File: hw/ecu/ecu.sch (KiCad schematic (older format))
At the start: 66 parts, among them J1 POWER, J2 UART_DEBUG, J3 DEBUG, J4 EXPANSION, J5 SWD, J6 CAN, J7 USB_B_Micro, SW1 RESET, U1 M24C64, U2 STM32F072RBTx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

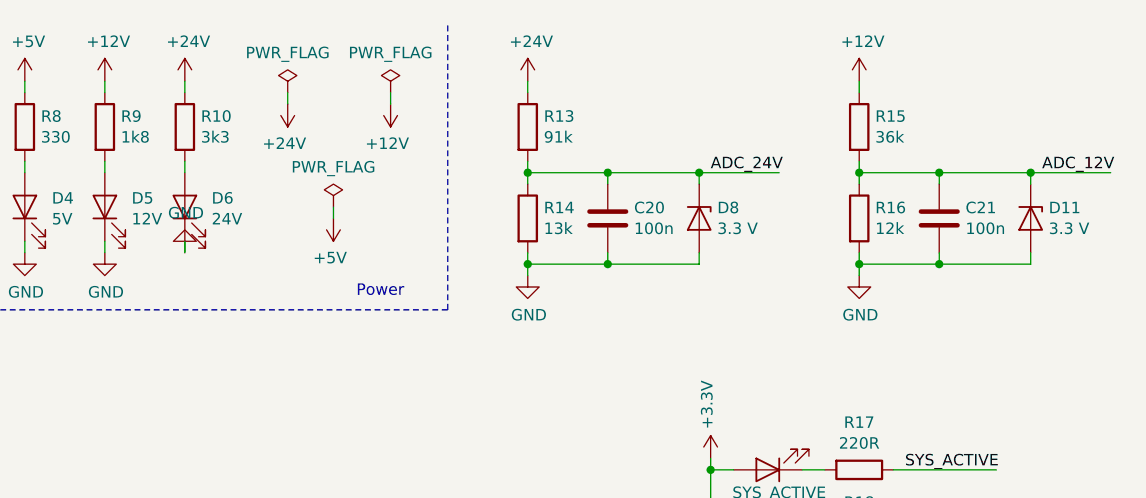
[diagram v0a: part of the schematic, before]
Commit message: Updated few resistors/capacitors values on board
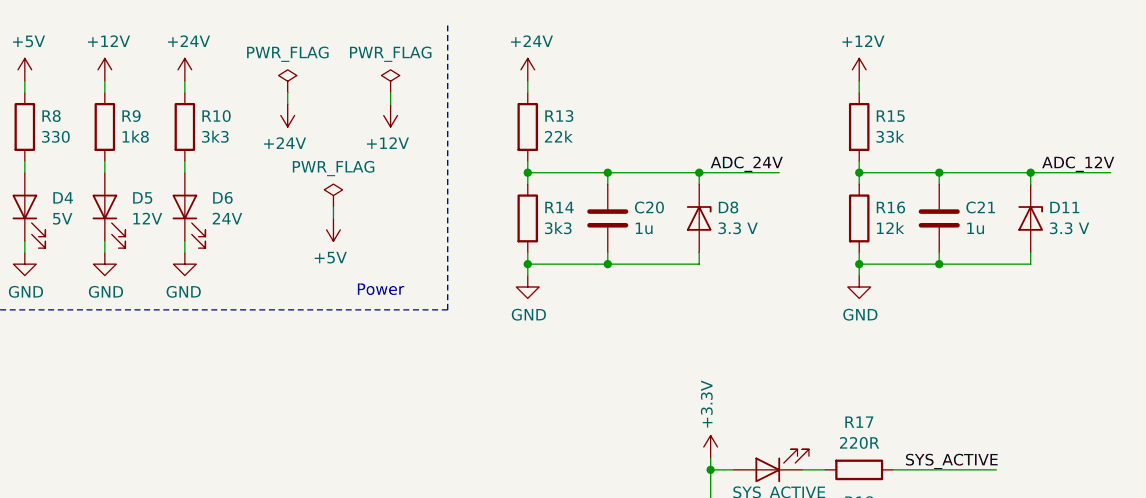
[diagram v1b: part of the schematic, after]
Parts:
- C20, C21: value 100n -> 1u
- R13: value 91k -> 22k
- R14: value 13k -> 3k3
- R15: value 36k -> 33k
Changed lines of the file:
@@
 F 3 "" H 7100 1500 50  0001 C CNN
 	1    7100 1500
-	1    0    0    1
+	-1   0    0    -1
 $EndComp
 Wire Wire Line
@@
 P 8600 950
 F 0 "R13" H 8670 996 50  0000 L CNN
-F 1 "91k" H 8670 905 50  0000 L CNN
+F 1 "22k" H 8670 905 50  0000 L CNN
 F 2 "Resistor_SMD:R_0805_2012Metric" V 8530 950 50  0001 C CNN
 F 3 "~" H 8600 950 50  0001 C CNN
@@
 P 8600 1350
 F 0 "R14" H 8670 1396 50  0000 L CNN
-F 1 "13k" H 8670 1305 50  0000 L CNN
+F 1 "3k3" H 8670 1305 50  0000 L CNN
 F 2 "Resistor_SMD:R_0805_2012Metric" V 8530 1350 50  0001 C CNN
 F 3 "~" H 8600 1350 50  0001 C CNN
@@
 P 8950 1350
 F 0 "C20" H 9065 1396 50  0000 L CNN
-F 1 "100n" H 9065 1305 50  0000 L CNN
+F 1 "1u" H 9065 1305 50  0000 L CNN
 F 2 "Capacitor_SMD:C_0805_2012Metric" H 8988 1200 50  0001 C CNN
 F 3 "~" H 8950 1350 50  0001 C CNN
@@
 P 10050 950
 F 0 "R15" H 10120 996 50  0000 L CNN
-F 1 "36k" H 10120 905 50  0000 L CNN
+F 1 "33k" H 10120 905 50  0000 L CNN
 F 2 "Resistor_SMD:R_0805_2012Metric" V 9980 950 50  0001 C CNN
 F 3 "~" H 10050 950 50  0001 C CNN
@@
 P 10400 1350
 F 0 "C21" H 10515 1396 50  0000 L CNN
-F 1 "100n" H 10515 1305 50  0000 L CNN
+F 1 "1u" H 10515 1305 50  0000 L CNN
 F 2 "Capacitor_SMD:C_0805_2012Metric" H 10438 1200 50  0001 C CNN
 F 3 "~" H 10400 1350 50  0001 C CNN

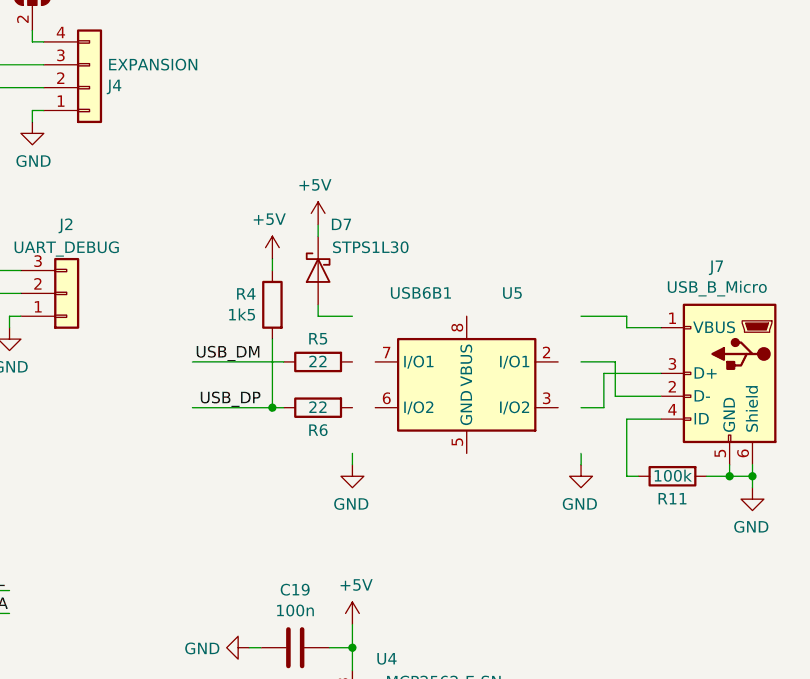
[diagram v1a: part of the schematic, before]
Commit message: Updated schematic to latest changes in usb protection ic
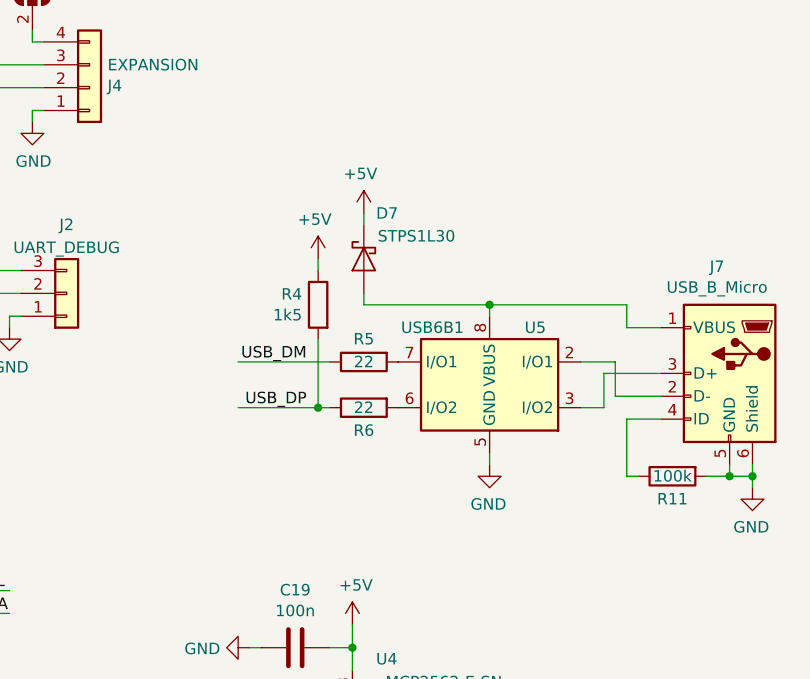
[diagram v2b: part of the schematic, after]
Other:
- moved on the sheet: D7, R4, R5, R6, U5
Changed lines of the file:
@@
 L Device:R R5
 U 1 1 5BB485B5
-P 5750 3700
-F 0 "R5" V 5650 3700 50  0000 C CNN
-F 1 "22" V 5750 3700 50  0000 C CNN
-F 2 "Resistor_SMD:R_0805_2012Metric" V 5680 3700 50  0001 C CNN
-F 3 "~" H 5750 3700 50  0001 C CNN
-	1    5750 3700
+P 5950 3700
+F 0 "R5" V 5850 3700 50  0000 C CNN
+F 1 "22" V 5950 3700 50  0000 C CNN
+F 2 "Resistor_SMD:R_0805_2012Metric" V 5880 3700 50  0001 C CNN
+F 3 "~" H 5950 3700 50  0001 C CNN
+	1    5950 3700
 	0    -1   1    0
 $EndComp
@@
 L Device:R R6
 U 1 1 5BB48786
-P 5750 3900
-F 0 "R6" V 5850 3900 50  0000 C CNN
-F 1 "22" V 5750 3900 50  0000 C CNN
-F 2 "Resistor_SMD:R_0805_2012Metric" V 5680 3900 50  0001 C CNN
-F 3 "~" H 5750 3900 50  0001 C CNN
-	1    5750 3900
+P 5950 3900
+F 0 "R6" V 6050 3900 50  0000 C CNN
+F 1 "22" V 5950 3900 50  0000 C CNN
+F 2 "Resistor_SMD:R_0805_2012Metric" V 5880 3900 50  0001 C CNN
+F 3 "~" H 5950 3900 50  0001 C CNN
+	1    5950 3900
 	0    -1   1    0
 $EndComp
-Text Label 5500 3700 2    50   ~ 0
+Text Label 5700 3700 2    50   ~ 0
 USB_DM
 Wire Wire Line
-	5600 3900 5550 3900
-Text Label 5500 3900 2    50   ~ 0
+	5800 3900 5750 3900
+Text Label 5700 3900 2    50   ~ 0
 USB_DP
 $Comp
@@
 L Device:R R4
 U 1 1 5BCA1E94
-P 5550 3450
-F 0 "R4" H 5620 3496 50  0000 L CNN
-F 1 "1k5" H 5620 3405 50  0000 L CNN
-F 2 "Resistor_SMD:R_0805_2012Metric" V 5480 3450 50  0001 C CNN
-F 3 "~" H 5550 3450 50  0001 C CNN
-	1    5550 3450
+P 5750 3450
+F 0 "R4" H 5820 3496 50  0000 L CNN
+F 1 "1k5" H 5820 3405 50  0000 L CNN
+F 2 "Resistor_SMD:R_0805_2012Metric" V 5680 3450 50  0001 C CNN
+F 3 "~" H 5750 3450 50  0001 C CNN
+	1    5750 3450
 	-1   0    0    -1
 $EndComp
@@
 L Power_Protection:USB6B1 U5
 U 1 1 5BFABEB9
-P 6400 3800
-F 0 "U5" H 6200 4200 50  0000 C CNN
-F 1 "USB6B1" H 6600 4200 50  0000 C CNN
-F 2 "Package_SO:SOIC-8_3.9x4.9mm_P1.27mm" H 5425 3400 50  0001 C CNN
-F 3 "http://www.st.com/content/ccc/resource/technical/document/datasheet/3e/ec/b2/54/b2/76/47/90/CD00001361.pdf/files/CD00001361.pdf/jcr:content/translations/en.CD00001361.pdf" H 5450 3700 50  0001 C CNN
-	1    6400 3800
-	-1   0    0    -1
-$EndComp
-$Comp
-L power:GND #PWR040
-U 1 1 5C0A5927
-P 5900 4150
-F 0 "#PWR040" H 5900 3900 50  0001 C CNN
-F 1 "GND" H 5905 3977 50  0000 C CNN
-F 2 "" H 5900 4150 50  0001 C CNN
-F 3 "" H 5900 4150 50  0001 C CNN
-	1    5900 4150
+P 6500 3800
+F 0 "U5" H 6300 4050 50  0000 C CNN
+F 1 "USB6B1" H 6750 4050 50  0000 C CNN
+F 2 "Package_SO:SOIC-8_3.9x4.9mm_P1.27mm" H 5525 3400 50  0001 C CNN
+F 3 "http://www.st.com/content/ccc/resource/technical/document/datasheet/3e/ec/b2/54/b2/76/47/90/CD00001361.pdf/files/CD00001361.pdf/jcr:content/translations/en.CD00001361.pdf" H 5550 3700 50  0001 C CNN
+	1    6500 3800
 	-1   0    0    -1
 $EndComp
@@
 L power:+5V #PWR039
 U 1 1 5C14EFB2
-P 5550 3250
-F 0 "#PWR039" H 5550 3100 50  0001 C CNN
-F 1 "+5V" H 5565 3423 50  0000 C CNN
-F 2 "" H 5550 3250 50  0001 C CNN
-F 3 "" H 5550 3250 50  0001 C CNN
-	1    5550 3250
+P 5750 3250
+F 0 "#PWR039" H 5750 3100 50  0001 C CNN
+F 1 "+5V" H 5765 3423 50  0000 C CNN
+F 2 "" H 5750 3250 50  0001 C CNN
+F 3 "" H 5750 3250 50  0001 C CNN
+	1    5750 3250
 	-1   0    0    -1
 $EndComp
@@
 L Device:D_Schottky D7
 U 1 1 5C457FB3
-P 5750 3300
-F 0 "D7" V 5550 3150 50  0000 L CNN
-F 1 "STPS1L30" V 5650 2900 50  0000 L CNN
-F 2 "Diode_SMD:D_SMB" H 5750 3300 50  0001 C CNN
-F 3 "~" H 5750 3300 50  0001 C CNN
-	1    5750 3300
+P 5950 3250
+F 0 "D7" V 5750 3100 50  0000 L CNN
+F 1 "STPS1L30" V 5850 2850 50  0000 L CNN
+F 2 "Diode_SMD:D_SMB" H 5950 3250 50  0001 C CNN
+F 3 "~" H 5950 3250 50  0001 C CNN
+	1    5950 3250
 	0    -1   1    0
 $EndComp
 Wire Wire Line
-	5900 3500 5750 3500
-Wire Wire Line
-	5750 3500 5750 3450
+	5950 3450 5950 3400
 $Comp
 L power:+5V #PWR049
 U 1 1 5C4B24B6
-P 5750 3100
-F 0 "#PWR049" H 5750 2950 50  0001 C CNN
-F 1 "+5V" H 5765 3273 50  0000 C CNN
-F 2 "" H 5750 3100 50  0001 C CNN
-F 3 "" H 5750 3100 50  0001 C CNN
-	1    5750 3100
+P 5950 3050
+F 0 "#PWR049" H 5950 2900 50  0001 C CNN
+F 1 "+5V" H 5965 3223 50  0000 C CNN
+F 2 "" H 5950 3050 50  0001 C CNN
+F 3 "" H 5950 3050 50  0001 C CNN
+	1    5950 3050
 	-1   0    0    -1
 $EndComp
 Wire Wire Line
-	5750 3100 5750 3150
+	5950 3050 5950 3100
 $Comp
 L Device:D_Schottky D1
@@
 NoConn ~ 3100 4400
 Wire Wire Line
-	5550 3250 5550 3300
+	5750 3250 5750 3300
 $Comp
 L power:GND #PWR0135
 U 1 1 5BEB994E
-P 6900 4150
-F 0 "#PWR0135" H 6900 3900 50  0001 C CNN
-F 1 "GND" H 6905 3977 50  0000 C CNN
-F 2 "" H 6900 4150 50  0001 C CNN
-F 3 "" H 6900 4150 50  0001 C CNN
-	1    6900 4150
+P 6500 4150
+F 0 "#PWR0135" H 6500 3900 50  0001 C CNN
+F 1 "GND" H 6505 3977 50  0000 C CNN
+F 2 "" H 6500 4150 50  0001 C CNN
+F 3 "" H 6500 4150 50  0001 C CNN
+	1    6500 4150
 	-1   0    0    -1
 $EndComp
 Wire Wire Line
-	6900 3500 7100 3500
-Wire Wire Line
-	7100 3500 7100 3550
-Wire Wire Line
 	7100 3550 7250 3550
 Wire Wire Line
-	6900 4150 6900 4100
-Wire Wire Line
-	5900 4100 5900 4150
-Wire Wire Line
 	7000 3750 7000 3900
 Wire Wire Line
@@
 	7050 3850 7250 3850
 Wire Wire Line
-	5200 3700 5600 3700
-Wire Wire Line
-	5550 3600 5550 3900
-Connection ~ 5550 3900
-Wire Wire Line
-	5550 3900 5200 3900
+	5400 3700 5800 3700
+Wire Wire Line
+	5750 3600 5750 3900
+Connection ~ 5750 3900
+Wire Wire Line
+	5750 3900 5400 3900
 $Comp
 L Device:D D55
@@
 Wire Wire Line
 	3200 600  3200 950
+Wire Wire Line
+	5950 3450 6500 3450
+Wire Wire Line
+	7100 3450 7100 3550
+Wire Wire Line
+	6500 3500 6500 3450
+Connection ~ 6500 3450
+Wire Wire Line
+	6500 3450 7100 3450
+Wire Wire Line
+	6500 4150 6500 4100
 $EndSCHEMATC

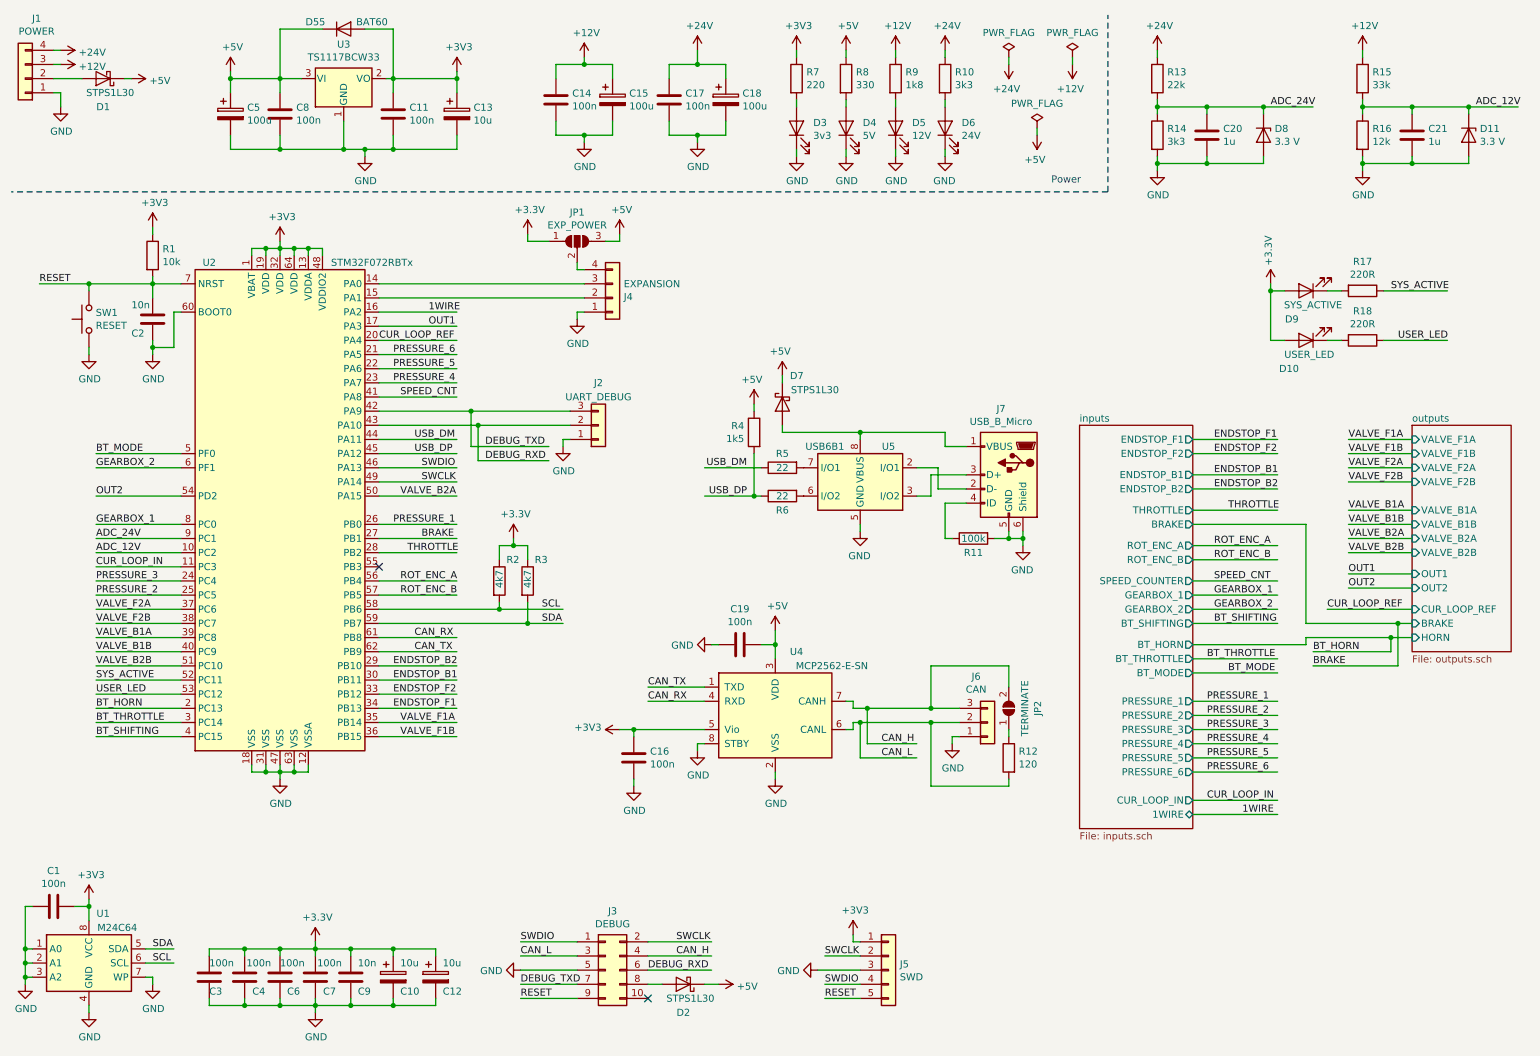
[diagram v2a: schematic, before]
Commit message: Added crystal for all can equipped boards
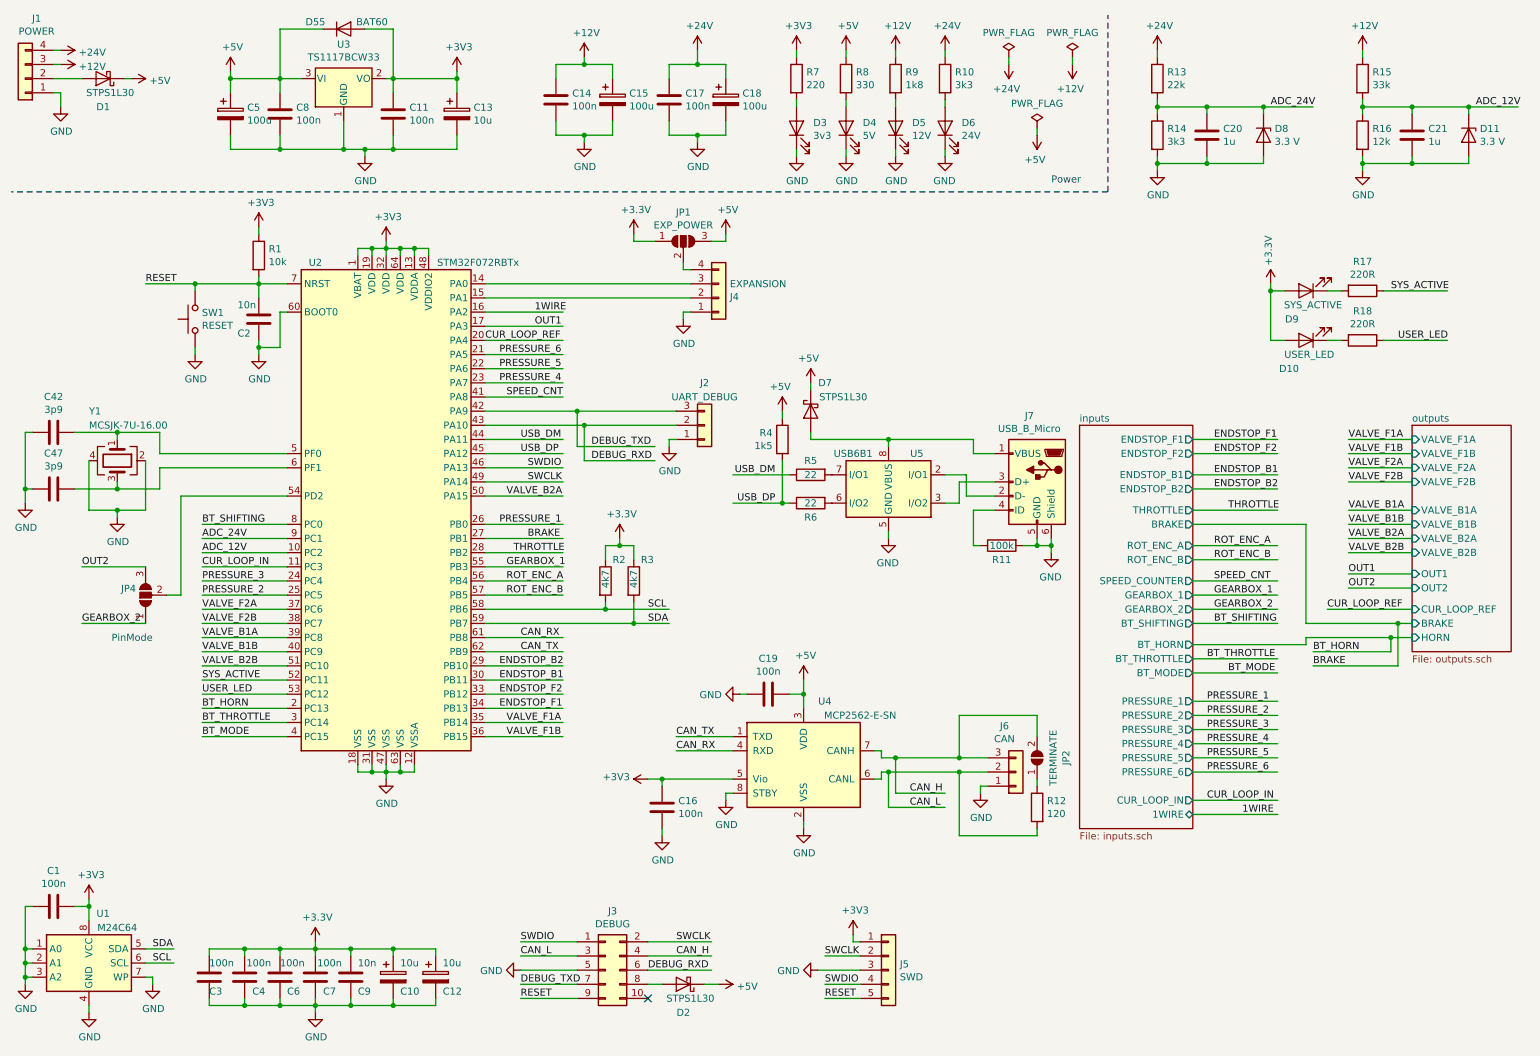
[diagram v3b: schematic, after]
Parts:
- added C42, C47: 3p9, Capacitor_SMD:C_0805_2012Metric, symbol Device:C
- added JP4: PinMode, Jumper:SolderJumper-3_P1.3mm_Open_Pad1.0x1.5mm, symbol Jumper:SolderJumper_3_Open
- added Y1: MCSJK-7U-16.00, Crystal:Crystal_SMD_3225-4Pin_3.2x2.5mm, symbol Device:Crystal_GND24
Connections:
- wire segments 379 -> 401
- no-connect marks 2 -> 1
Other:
- moved on the sheet: C16, C19, C2, D7, J2, J4, J6, J7, JP1, JP2, R1, R11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
